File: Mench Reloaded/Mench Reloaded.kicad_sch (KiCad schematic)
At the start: 22 parts, among them IC1 DS1813, SW1 SW_Push, U1 W65C265SxQ, Y1 32.768 kHz, Y2 3.6864 mHz

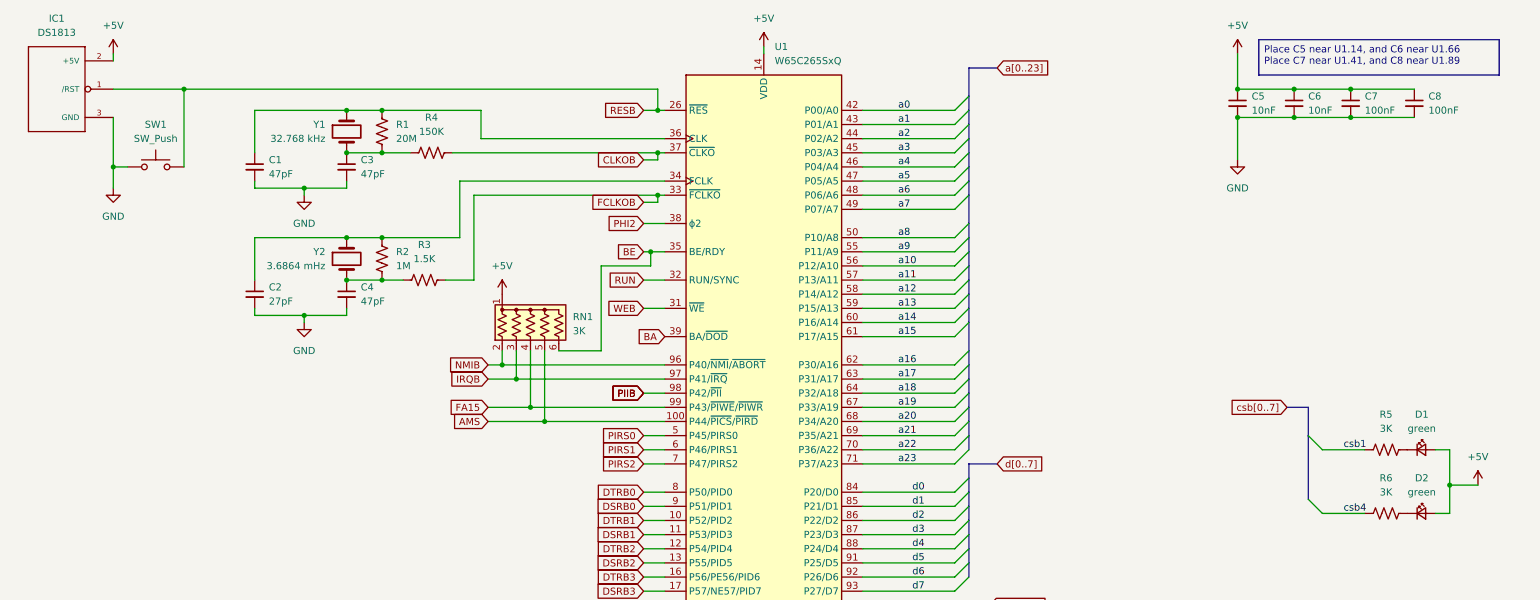
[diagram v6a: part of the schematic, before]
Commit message: Added power selector header (ftdi vs battery). Added 128kB vs 256kB RAM selector. Added pull up for RESB and DS1813. Reworked traces at top of the board using streets and avenues.
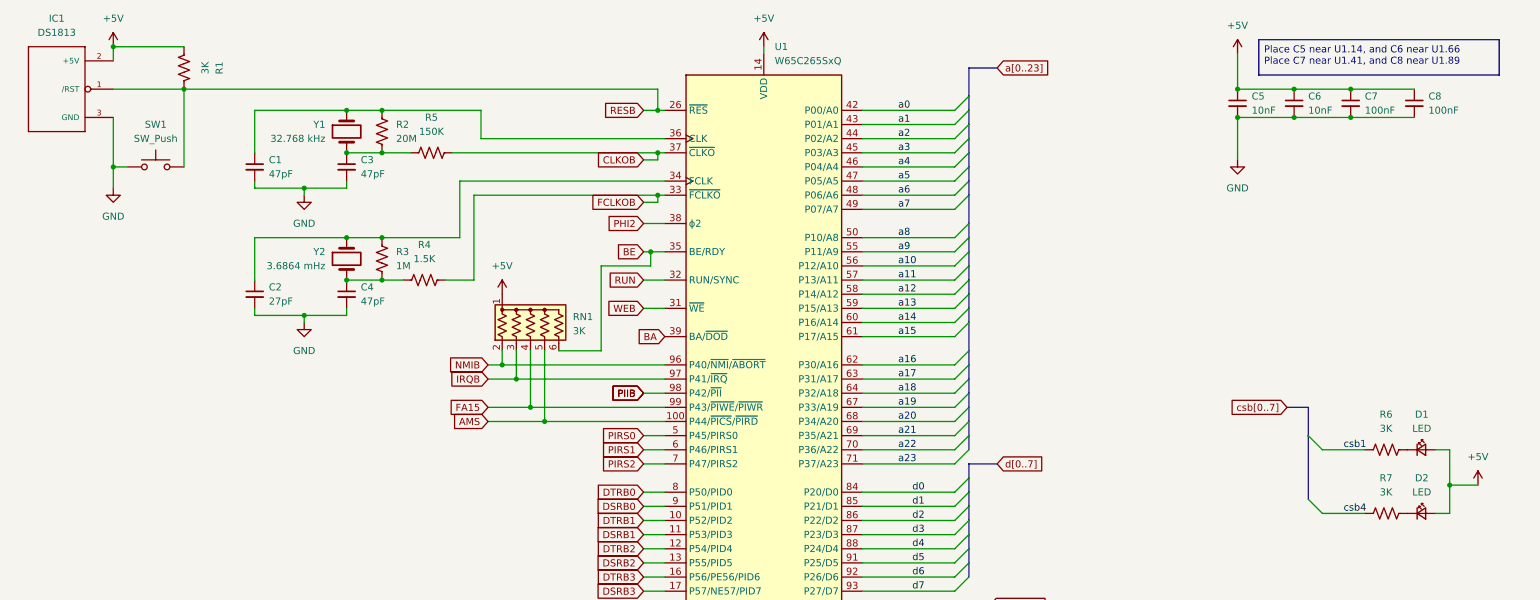
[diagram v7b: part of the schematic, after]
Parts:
- added R1: 3K, Resistor_SMD:R_0805_2012Metric_Pad1.20x1.40mm_HandSolder, symbol Device:R_US
- D1, D2: value green -> LED
- renumbered R1 to R2, R2 to R3, R3 to R4, R4 to R5, R5 to R6, R6 to R7
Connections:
- net +5V: now also R1.2
- net RESB: now also R1.1
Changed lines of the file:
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@@
 	)
 	(junction
+		(at 31.75 19.05)
+		(diameter 0)
+		(color 0 0 0 0)
+	)
+	(junction
 		(at 31.75 40.64)
 		(diameter 0)
@@
 	(wire
 		(pts
+			(xy 44.45 19.05) (xy 31.75 19.05)
+		)
+		(stroke
+			(width 0)
+			(type default)
+		)
+	)
+	(wire
+		(pts
 			(xy 66.04 67.31) (xy 66.04 68.58)
 		)
@@
 		)
 	)
-	(wire
-		(pts
-			(xy 31.75 20.32) (xy 31.75 21.59)
-		)
-		(stroke
-			(width 0)
-			(type default)
-		)
-	)
 	(bus
 		(pts
@@
 		)
 	)
+	(wire
+		(pts
+			(xy 31.75 19.05) (xy 31.75 21.59)
+		)
+		(stroke
+			(width 0)
+			(type default)
+		)
+	)
 	(bus
 		(pts
@@
 	(symbol
 		(lib_id "power:+5V")
-		(at 31.75 20.32 0)
+		(at 31.75 19.05 0)
 		(unit 1)
 		(exclude_from_sim no)
@@
 		(on_board yes)
 		(dnp no)
-		(fields_autoplaced yes)
 		(property "Reference" "#PWR01"
-			(at 31.75 24.13 0)
+			(at 31.75 22.86 0)
 			(effects
 				(font
@@
 		)
 		(property "Value" "+5V"
-			(at 31.75 15.24 0)
+			(at 31.75 13.97 0)
 			(effects
 				(font
@@
 		)
 		(property "Footprint" ""
-			(at 31.75 20.32 0)
+			(at 31.75 19.05 0)
 			(effects
 				(font
@@
 		)
 		(property "Datasheet" ""
-			(at 31.75 20.32 0)
+			(at 31.75 19.05 0)
 			(effects
 				(font
@@
 		)
 		(property "Description" ""
-			(at 31.75 20.32 0)
+			(at 31.75 19.05 0)
 			(effects
 				(font
@@
 			)
 		)
-		(property "Value" "green"
+		(property "Value" "LED"
 			(at 266.7635 87.63 0)
 			(effects
@@
 	(symbol
 		(lib_id "Device:R_US")
-		(at 80.01 34.29 180)
+		(at 44.45 22.86 0)
+		(mirror x)
 		(unit 1)
 		(exclude_from_sim no)
@@
 		(fields_autoplaced yes)
 		(property "Reference" "R1"
+			(at 50.8 22.86 90)
+			(effects
+				(font
+					(size 1.27 1.27)
+				)
+			)
+		)
+		(property "Value" "3K"
+			(at 48.26 22.86 90)
+			(effects
+				(font
+					(size 1.27 1.27)
+				)
+			)
+		)
+		(property "Footprint" "Resistor_SMD:R_0805_2012Metric_Pad1.20x1.40mm_HandSolder"
+			(at 45.466 22.606 90)
+			(effects
+				(font
+					(size 1.27 1.27)
+				)
+				(hide yes)
+			)
+		)
+		(property "Datasheet" "~"
+			(at 44.45 22.86 0)
+			(effects
+				(font
+					(size 1.27 1.27)
+				)
+				(hide yes)
+			)
+		)
+		(property "Description" ""
+			(at 44.45 22.86 0)
+			(effects
+				(font
+					(size 1.27 1.27)
+				)
+			)
+		)
+		(pin "1"
+		)
+		(pin "2"
+		)
+		(instances
+			(project "Mench Reloaded"
+				(path "/e63e39d7-6ac0-4ffd-8aa3-1841a4541b55"
+					(reference "R1")
+					(unit 1)
+				)
+			)
+		)
+	)
+	(symbol
+		(lib_id "Device:R_US")
+		(at 80.01 34.29 180)
+		(unit 1)
+		(exclude_from_sim no)
+		(in_bom yes)
+		(on_board yes)
+		(dnp no)
+		(fields_autoplaced yes)
+		(property "Reference" "R2"
 			(at 82.55 33.02 0)
 			(effects
@@
 			(project "Mench Reloaded"
 				(path "/e63e39d7-6ac0-4ffd-8aa3-1841a4541b55"
-					(reference "R1")
+					(reference "R2")
 					(unit 1)
 				)
@@
 		(dnp no)
 		(fields_autoplaced yes)
-		(property "Reference" "R4"
+		(property "Reference" "R5"
 			(at 88.9 31.75 90)
 			(effects
@@
 			(project "Mench Reloaded"
 				(path "/e63e39d7-6ac0-4ffd-8aa3-1841a4541b55"
-					(reference "R4")
+					(reference "R5")
 					(unit 1)
 				)
@@
 		(dnp no)
 		(fields_autoplaced yes)
-		(property "Reference" "R5"
+		(property "Reference" "R6"
 			(at 260.35 85.09 90)
 			(effects
@@
 			(project "Mench Reloaded"
 				(path "/e63e39d7-6ac0-4ffd-8aa3-1841a4541b55"
-					(reference "R5")
+					(reference "R6")
 					(unit 1)
 				)
@@
 		(dnp no)
 		(fields_autoplaced yes)
-		(property "Reference" "R6"
+		(property "Reference" "R7"
 			(at 260.35 96.52 90)
 			(effects
@@
 			(project "Mench Reloaded"
 				(path "/e63e39d7-6ac0-4ffd-8aa3-1841a4541b55"
-					(reference "R6")
+					(reference "R7")
 					(unit 1)
 				)
@@
 		(dnp no)
 		(fields_autoplaced yes)
-		(property "Reference" "R3"
+		(property "Reference" "R4"
 			(at 87.63 54.61 90)
 			(effects
@@
 			(project "Mench Reloaded"
 				(path "/e63e39d7-6ac0-4ffd-8aa3-1841a4541b55"
-					(reference "R3")
+					(reference "R4")
 					(unit 1)
 				)
@@
 			)
 		)
-		(property "Value" "green"
+		(property "Value" "LED"
 			(at 266.7635 99.06 0)
 			(effects
@@
 		(dnp no)
 		(fields_autoplaced yes)
-		(property "Reference" "R2"
+		(property "Reference" "R3"
 			(at 82.55 55.88 0)
 			(effects
@@
 			(project "Mench Reloaded"
 				(path "/e63e39d7-6ac0-4ffd-8aa3-1841a4541b55"
-					(reference "R2")
+					(reference "R3")
 					(unit 1)
 				)

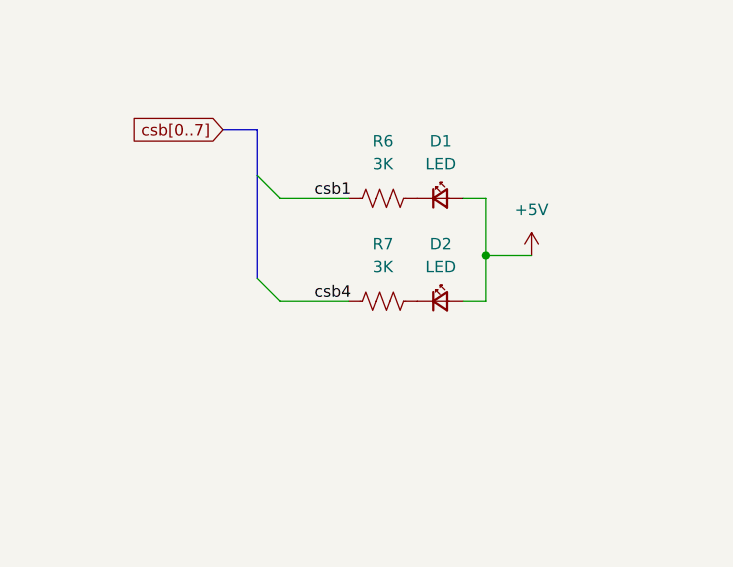
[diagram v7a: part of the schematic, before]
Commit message: Moved EEPROM North to create more space for traces. Reworked all traces from CPU to fix rats nest wiring. Added LED to csb2 to allow for debugging when internal bus is used. Added to list of signal net classes to make consistant data traces.
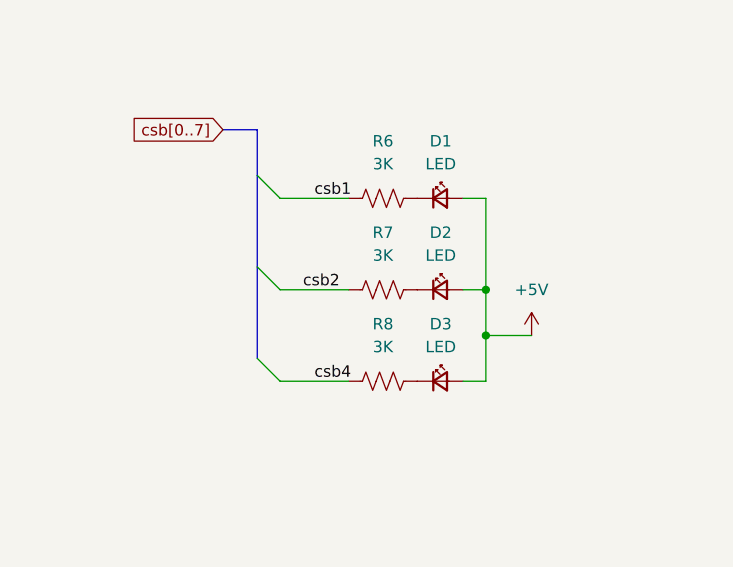
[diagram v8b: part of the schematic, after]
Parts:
- added D2: LED, LED_SMD:LED_0805_2012Metric_Pad1.15x1.40mm_HandSolder, symbol Device:LED_Small
- added R7: 3K, Resistor_SMD:R_0805_2012Metric_Pad1.20x1.40mm_HandSolder, symbol Device:R_US
- renumbered D2 to D3, R7 to R8
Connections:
- net +5V: now also D2.2 (A)
- net csb2: now also R7.1
- new net: D2.1 (K), R7.2
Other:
- moved on the sheet: D3, R8
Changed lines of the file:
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@@
 	)
 	(junction
+		(at 271.78 101.6)
+		(diameter 0)
+		(color 0 0 0 0)
+	)
+	(junction
 		(at 129.54 38.1)
 		(diameter 0)
@@
 	)
 	(junction
-		(at 271.78 97.79)
+		(at 271.78 106.68)
 		(diameter 0)
 		(color 0 0 0 0)
@@
 	)
 	(bus_entry
-		(at 246.38 100.33)
+		(at 246.38 109.22)
 		(size 2.54 2.54)
 		(stroke
@@
 	)
 	(bus_entry
+		(at 246.38 99.06)
+		(size 2.54 2.54)
+		(stroke
+			(width 0)
+			(type default)
+		)
+	)
+	(bus_entry
 		(at 185.42 132.08)
 		(size -2.54 2.54)
@@
 	(wire
 		(pts
-			(xy 271.78 97.79) (xy 271.78 102.87)
+			(xy 271.78 106.68) (xy 271.78 111.76)
 		)
 		(stroke
@@
 	(wire
 		(pts
-			(xy 248.92 102.87) (xy 256.54 102.87)
+			(xy 248.92 111.76) (xy 256.54 111.76)
 		)
 		(stroke
@@
 		)
 	)
+	(wire
+		(pts
+			(xy 248.92 101.6) (xy 256.54 101.6)
+		)
+		(stroke
+			(width 0)
+			(type default)
+		)
+	)
 	(bus
 		(pts
@@
 	(bus
 		(pts
+			(xy 246.38 99.06) (xy 246.38 109.22)
+		)
+		(stroke
+			(width 0)
+			(type default)
+		)
+	)
+	(bus
+		(pts
 			(xy 185.42 109.22) (xy 185.42 111.76)
 		)
@@
 	(bus
 		(pts
-			(xy 246.38 88.9) (xy 246.38 100.33)
+			(xy 246.38 88.9) (xy 246.38 99.06)
 		)
 		(stroke
@@
 		)
 	)
+	(wire
+		(pts
+			(xy 271.78 101.6) (xy 269.24 101.6)
+		)
+		(stroke
+			(width 0)
+			(type default)
+		)
+	)
 	(bus
 		(pts
@@
 	(wire
 		(pts
-			(xy 271.78 91.44) (xy 271.78 97.79)
+			(xy 271.78 91.44) (xy 271.78 101.6)
 		)
 		(stroke
@@
 	(wire
 		(pts
-			(xy 269.24 102.87) (xy 271.78 102.87)
+			(xy 269.24 111.76) (xy 271.78 111.76)
 		)
 		(stroke
@@
 	(wire
 		(pts
-			(xy 271.78 97.79) (xy 276.86 97.79)
+			(xy 271.78 106.68) (xy 276.86 106.68)
 		)
 		(stroke
@@
 	(wire
 		(pts
+			(xy 271.78 101.6) (xy 271.78 106.68)
+		)
+		(stroke
+			(width 0)
+			(type default)
+		)
+	)
+	(wire
+		(pts
 			(xy 57.15 44.45) (xy 66.04 44.45)
 		)
@@
 	)
 	(label "csb4"
-		(at 252.73 102.87 0)
+		(at 252.73 111.76 0)
 		(effects
 			(font
@@
 		)
 	)
+	(label "csb2"
+		(at 251.46 101.6 0)
+		(effects
+			(font
+				(size 1.27 1.27)
+			)
+			(justify left bottom)
+		)
+	)
 	(label "a12"
 		(at 172.72 63.5 0)
@@
 	(symbol
 		(lib_id "Device:R_US")
-		(at 260.35 102.87 90)
+		(at 260.35 111.76 90)
 		(unit 1)
 		(exclude_from_sim no)
@@
 		(dnp no)
 		(fields_autoplaced yes)
-		(property "Reference" "R7"
-			(at 260.35 96.52 90)
+		(property "Reference" "R8"
+			(at 260.35 105.41 90)
 			(effects
 				(font
@@
 		)
 		(property "Value" "3K"
-			(at 260.35 99.06 90)
+			(at 260.35 107.95 90)
 			(effects
 				(font
@@
 		)
 		(property "Footprint" "Resistor_SMD:R_0805_2012Metric_Pad1.20x1.40mm_HandSolder"
-			(at 260.604 101.854 90)
+			(at 260.604 110.744 90)
 			(effects
 				(font
@@
 		)
 		(property "Datasheet" "~"
-			(at 260.35 102.87 0)
+			(at 260.35 111.76 0)
 			(effects
 				(font
@@
 		)
 		(property "Description" ""
-			(at 260.35 102.87 0)
+			(at 260.35 111.76 0)
 			(effects
 				(font
@@
 			(project "Mench Reloaded"
 				(path "/e63e39d7-6ac0-4ffd-8aa3-1841a4541b55"
-					(reference "R7")
+					(reference "R8")
 					(unit 1)
 				)
@@
 	(symbol
 		(lib_id "Device:R_US")
+		(at 260.35 101.6 90)
+		(unit 1)
+		(exclude_from_sim no)
+		(in_bom yes)
+		(on_board yes)
+		(dnp no)
+		(fields_autoplaced yes)
+		(property "Reference" "R7"
+			(at 260.35 95.25 90)
+			(effects
+				(font
+					(size 1.27 1.27)
+				)
+			)
+		)
+		(property "Value" "3K"
+			(at 260.35 97.79 90)
+			(effects
+				(font
+					(size 1.27 1.27)
+				)
+			)
+		)
+		(property "Footprint" "Resistor_SMD:R_0805_2012Metric_Pad1.20x1.40mm_HandSolder"
+			(at 260.604 100.584 90)
+			(effects
+				(font
+					(size 1.27 1.27)
+				)
+				(hide yes)
+			)
+		)
+		(property "Datasheet" "~"
+			(at 260.35 101.6 0)
+			(effects
+				(font
+					(size 1.27 1.27)
+				)
+				(hide yes)
+			)
+		)
+		(property "Description" ""
+			(at 260.35 101.6 0)
+			(effects
+				(font
+					(size 1.27 1.27)
+				)
+			)
+		)
+		(pin "1"
+		)
+		(pin "2"
+		)
+		(instances
+			(project "Mench Reloaded"
+				(path "/e63e39d7-6ac0-4ffd-8aa3-1841a4541b55"
+					(reference "R7")
+					(unit 1)
+				)
+			)
+		)
+	)
+	(symbol
+		(lib_id "Device:R_US")
 		(at 87.63 60.96 90)
 		(unit 1)
@@
 	(symbol
 		(lib_id "power:+5V")
-		(at 276.86 97.79 0)
+		(at 276.86 106.68 0)
 		(unit 1)
 		(exclude_from_sim no)
@@
 		(fields_autoplaced yes)
 		(property "Reference" "#PWR010"
-			(at 276.86 101.6 0)
+			(at 276.86 110.49 0)
 			(effects
 				(font
@@
 		)
 		(property "Value" "+5V"
-			(at 276.86 92.71 0)
+			(at 276.86 101.6 0)
 			(effects
 				(font
@@
 		)
 		(property "Footprint" ""
-			(at 276.86 97.79 0)
+			(at 276.86 106.68 0)
 			(effects
 				(font
@@
 		)
 		(property "Datasheet" ""
-			(at 276.86 97.79 0)
+			(at 276.86 106.68 0)
 			(effects
 				(font
@@
 		)
 		(property "Description" ""
-			(at 276.86 97.79 0)
+			(at 276.86 106.68 0)
 			(effects
 				(font
@@
 	(symbol
 		(lib_id "Device:LED_Small")
-		(at 266.7 102.87 0)
+		(at 266.7 111.76 0)
 		(unit 1)
 		(exclude_from_sim no)
@@
 		(on_board yes)
 		(dnp no)
-		(property "Reference" "D2"
-			(at 266.7635 96.52 0)
+		(property "Reference" "D3"
+			(at 266.7635 105.41 0)
 			(effects
 				(font
@@
 		)
 		(property "Value" "LED"
-			(at 266.7635 99.06 0)
+			(at 266.7635 107.95 0)
 			(effects
 				(font
@@
 		)
 		(property "Footprint" "LED_SMD:LED_0805_2012Metric_Pad1.15x1.40mm_HandSolder"
-			(at 266.7 102.87 90)
+			(at 266.7 111.76 90)
 			(effects
 				(font
@@
 		)
 		(property "Datasheet" "~"
-			(at 266.7 102.87 90)
+			(at 266.7 111.76 90)
 			(effects
 				(font
@@
 		)
 		(property "Description" ""
-			(at 266.7 102.87 0)
+			(at 266.7 111.76 0)
 			(effects
 				(font
@@
 			(project "Mench Reloaded"
 				(path "/e63e39d7-6ac0-4ffd-8aa3-1841a4541b55"
-					(reference "D2")
+					(reference "D3")
 					(unit 1)
 				)
@@
 					(unit 1)
 				)
+			)
+		)
+	)
+	(symbol
+		(lib_id "Device:LED_Small")
+		(at 266.7 101.6 0)
+		(unit 1)
+		(exclude_from_sim no)
+		(in_bom yes)
+		(on_board yes)
+		(dnp no)
+		(property "Reference" "D2"
+			(at 266.7635 95.25 0)
+			(effects
+				(font
+					(size 1.27 1.27)
+				)
+			)
+		)
+		(property "Value" "LED"
+			(at 266.7635 97.79 0)
+			(effects
+				(font
+					(size 1.27 1.27)
+				)
+			)
+		)
+		(property "Footprint" "LED_SMD:LED_0805_2012Metric_Pad1.15x1.40mm_HandSolder"
+			(at 266.7 101.6 90)
+			(effects
+				(font
+					(size 1.27 1.27)
+				)
+				(hide yes)
+			)
+		)
+		(property "Datasheet" "~"
+			(at 266.7 101.6 90)
+			(effects
+				(font
+					(size 1.27 1.27)
+				)
+				(hide yes)
+			)
+		)
+		(property "Description" ""
+			(at 266.7 101.6 0)
+			(effects
+				(font
+					(size 1.27 1.27)
+				)
+			)
+		)
+		(pin "1"
+		)
+		(pin "2"
+		)
+		(instances
+			(project "Mench Reloaded"
+				(path "/e63e39d7-6ac0-4ffd-8aa3-1841a4541b55"
+					(reference "D2")
+					(unit 1)
+				)
